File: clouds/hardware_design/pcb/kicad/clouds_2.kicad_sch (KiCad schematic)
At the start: 37 parts

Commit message: clouds wm8731 schematic update
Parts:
- IC8: value (none) -> WM8731; footprint (none) -> Package_DFN_QFN:QFN-28-1EP_5x5mm_P0.5mm_EP3.35x3.35mm
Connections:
- net +3V3: now also IC8.3 (DCVDD), IC8.5 (DBVDD); no longer IC8.1 (DBVDD), IC8.27 (DCVDD)
- net +3V3_A: now also IC8.12 (HPVDD), IC8.18 (AVDD); no longer IC8.14 (AVDD), IC8.8 (HPVDD)
- net GND: now also IC8.19 (AGND), IC8.25 (MODE), IC8.26 (CSB), IC8.4 (DGND); no longer IC8.11 (HPGND), IC8.21 (MODE), IC8.22 (CSB), IC8.28 (DGND)
- net I2C_SCL: now also IC8.28 (SCLK); no longer IC8.24 (SCLK)
- net I2C_SDA: now also IC8.27 (SDIN); no longer IC8.23 (SDIN)
- net I2S_LRCK: now also IC8.11 (ADCLRC), IC8.9 (DACLRC); no longer IC8.5 (DACLRC), IC8.7 (ADCLRC)
- net I2S_SCK: now also IC8.7 (BCLK); no longer IC8.3 (BCLK)
- net I2S_SIN: now also IC8.10 (ADCDAT); no longer IC8.6 (ADCDAT)
- net I2S_SOUT: now also IC8.8 (DACDAT); no longer IC8.4 (DACDAT)
- net LIN: now also IC8.24 (LLINEIN); no longer IC8.20 (LLINEIN)
- net LOUT: now also IC8.16 (LOUT); no longer IC8.12 (LOUT)
- net RIN: now also IC8.23 (RLINEIN); no longer IC8.19 (RLINEIN)
- net ROUT: now also IC8.17 (ROUT); no longer IC8.13 (ROUT)
- net at C48.2, Q4.2: now also IC8.1 (XTI/MCLK); no longer IC8.25 (XTI/MCLK)
- net at C47.2, Q4.1: now also IC8.2 (XTO); no longer IC8.26 (XTO)
- net at C34.1, C35.+: now also IC8.20 (VMID); no longer IC8.16 (VMID)
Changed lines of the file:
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@@
     (pin "6")
+  )
+  (symbol (lib_id "clouds-eagle-import:WM8731") (at 340.36 111.76 0) (unit 1)
+    (in_bom yes) (on_board yes)
+    (property "Reference" "IC8" (id 0) (at 327.66 85.09 0)
+      (effects (font (size 1.778 1.5113)) (justify left bottom))
+    )
+    (property "Value" "WM8731" (id 1) (at 340.36 111.76 0)
+      (effects (font (size 1.27 1.27)) hide)
+    )
+    (property "Footprint" "Package_DFN_QFN:QFN-28-1EP_5x5mm_P0.5mm_EP3.35x3.35mm" (id 2) (at 340.36 109.22 0)
+      (effects (font (size 1.27 1.27)) hide)
+    )
+    (property "Datasheet" "" (id 3) (at 340.36 111.76 0)
+      (effects (font (size 1.27 1.27)) hide)
+    )
+    (pin "1")
+    (pin "10")
+    (pin "11")
+    (pin "12")
+    (pin "13")
+    (pin "14")
+    (pin "15")
+    (pin "16")
+    (pin "17")
+    (pin "18")
+    (pin "19")
+    (pin "2")
+    (pin "20")
+    (pin "21")
+    (pin "22")
+    (pin "23")
+    (pin "24")
+    (pin "25")
+    (pin "26")
+    (pin "27")
+    (pin "28")
+    (pin "3")
+    (pin "4")
+    (pin "5")
+    (pin "6")
+    (pin "7")
+    (pin "8")
+    (pin "9")
   )
   (symbol (lib_id "clouds-eagle-import:EVQQ2") (at 71.12 187.96 0) (unit 1)
@@
     (pin "2")
   )
-  (symbol (lib_id "clouds-eagle-import:WM8731") (at 340.36 111.76 0) (unit 1)
-    (in_bom yes) (on_board yes)
-    (property "Reference" "IC8" (id 0) (at 327.66 85.09 0)
-      (effects (font (size 1.778 1.5113)) (justify left bottom))
-    )
-    (property "Value" "" (id 1) (at 340.36 111.76 0)
-      (effects (font (size 1.27 1.27)) hide)
-    )
-    (property "Footprint" "" (id 2) (at 340.36 111.76 0)
-      (effects (font (size 1.27 1.27)) hide)
-    )
-    (property "Datasheet" "" (id 3) (at 340.36 111.76 0)
-      (effects (font (size 1.27 1.27)) hide)
-    )
-    (pin "1")
-    (pin "10")
-    (pin "11")
-    (pin "12")
-    (pin "13")
-    (pin "14")
-    (pin "15")
-    (pin "16")
-    (pin "17")
-    (pin "18")
-    (pin "19")
-    (pin "2")
-    (pin "20")
-    (pin "21")
-    (pin "22")
-    (pin "23")
-    (pin "24")
-    (pin "25")
-    (pin "26")
-    (pin "27")
-    (pin "28")
-    (pin "3")
-    (pin "4")
-    (pin "5")
-    (pin "6")
-    (pin "7")
-    (pin "8")
-    (pin "9")
-  )
   (symbol (lib_id "clouds-eagle-import:C-USC0603") (at 195.58 200.66 0) (unit 1)

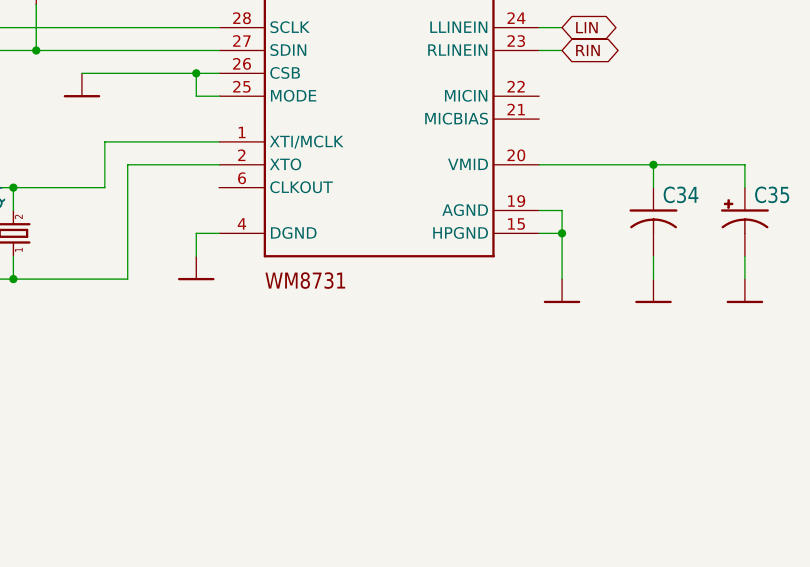
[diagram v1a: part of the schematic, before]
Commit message: clouds wm8731 QFN on PCB. also panasonic a -> b caps
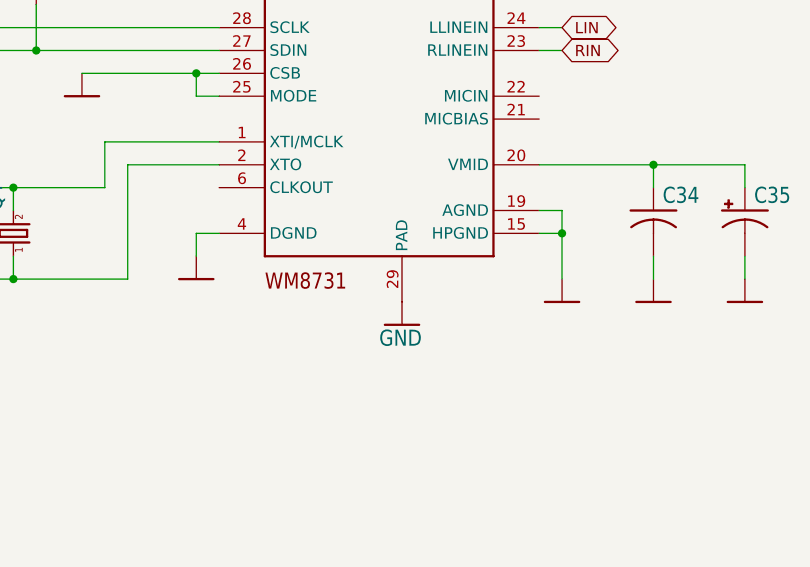
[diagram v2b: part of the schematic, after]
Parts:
- C28, C49: footprint (none) -> clouds:PANASONIC_B
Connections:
- net GND: now also IC8.29 (PAD)
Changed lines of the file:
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@@
+    (pin "1")
+  )
+  (symbol (lib_id "clouds-eagle-import:GND") (at 342.9 144.78 0) (unit 1)
+    (in_bom yes) (on_board yes)
+    (property "Reference" "#GND0101" (id 0) (at 342.9 144.78 0)
+      (effects (font (size 1.27 1.27)) hide)
+    )
+    (property "Value" "GND" (id 1) (at 340.36 147.32 0)
+      (effects (font (size 1.778 1.5113)) (justify left bottom))
+    )
+    (property "Footprint" "clouds:" (id 2) (at 342.9 144.78 0)
+      (effects (font (size 1.27 1.27)) hide)
+    )
+    (property "Datasheet" "" (id 3) (at 342.9 144.78 0)
+      (effects (font (size 1.27 1.27)) hide)
+    )
     (pin "1")
   )
@@
     (pin "3")
     (pin "4")
+    (pin "29")
     (pin "5")
     (pin "6")
@@
       (effects (font (size 1.778 1.5113)) (justify left bottom))
     )
-    (property "Footprint" "" (id 2) (at 215.9 200.66 0)
+    (property "Footprint" "clouds:PANASONIC_B" (id 2) (at 215.9 200.66 0)
       (effects (font (size 1.27 1.27)) hide)
     )
@@
       (effects (font (size 1.778 1.5113)) (justify left bottom))
     )
-    (property "Footprint" "" (id 2) (at 243.84 200.66 0)
-      (effects (font (size 1.27 1.27)) hide)
-    )
+    (property "Footprint" "clouds:PANASONIC_B" (id 2) (at 243.84 200.66 0)
+      (effects (font (size 1.27 1.27)) hide)
+    )

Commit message: clouds SMD reset + boot buttons
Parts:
- SW4, SW5: footprint (none) -> Supercell 1.3:k2-1808 pushbutton switch
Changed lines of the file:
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@@
       (effects (font (size 1.778 1.5113)) (justify left bottom))
     )
-    (property "Footprint" "" (id 2) (at 71.12 187.96 0)
+    (property "Footprint" "Supercell 1.3:k2-1808 pushbutton switch" (id 2) (at 71.12 187.96 0)
       (effects (font (size 1.27 1.27)) hide)
     )
@@
       (effects (font (size 1.778 1.5113)) (justify left bottom))
     )
-    (property "Footprint" "" (id 2) (at 73.66 160.02 0)
+    (property "Footprint" "Supercell 1.3:k2-1808 pushbutton switch" (id 2) (at 73.66 160.02 0)
       (effects (font (size 1.27 1.27)) hide)
     )

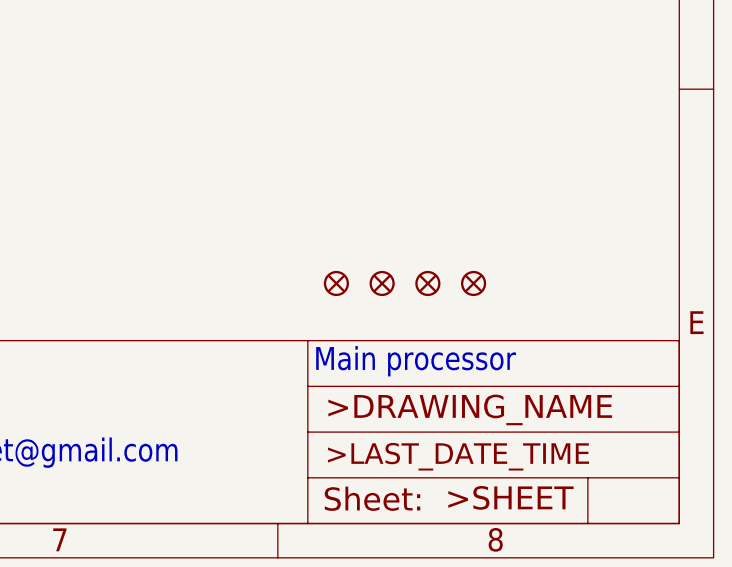
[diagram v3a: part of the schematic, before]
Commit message: clouds new kind of LED/switch pushbutton
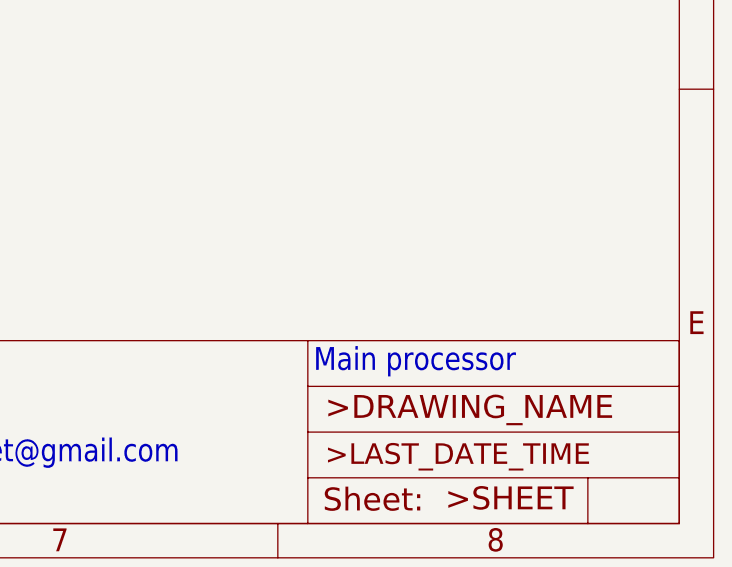
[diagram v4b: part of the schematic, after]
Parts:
- removed F1, F2, F3, F4: (no value), symbol clouds-eagle-import:FIDUCIAL1X2
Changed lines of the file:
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@@
     (pin "1")
-  )
-  (symbol (lib_id "clouds-eagle-import:FIDUCIAL1X2") (at 373.38 248.92 0) (unit 1)
-    (in_bom yes) (on_board yes)
-    (property "Reference" "F3" (id 0) (at 373.38 248.92 0)
-      (effects (font (size 1.27 1.27)) hide)
-    )
-    (property "Value" "" (id 1) (at 373.38 248.92 0)
-      (effects (font (size 1.27 1.27)) hide)
-    )
-    (property "Footprint" "" (id 2) (at 373.38 248.92 0)
-      (effects (font (size 1.27 1.27)) hide)
-    )
-    (property "Datasheet" "" (id 3) (at 373.38 248.92 0)
-      (effects (font (size 1.27 1.27)) hide)
-    )
   )
   (symbol (lib_id "clouds-eagle-import:CRYSTALHC49UP") (at 299.72 134.62 90) (unit 1)
@@
     (pin "1")
     (pin "2")
-  )
-  (symbol (lib_id "clouds-eagle-import:FIDUCIAL1X2") (at 378.46 248.92 0) (unit 1)
-    (in_bom yes) (on_board yes)
-    (property "Reference" "F2" (id 0) (at 378.46 248.92 0)
-      (effects (font (size 1.27 1.27)) hide)
-    )
-    (property "Value" "" (id 1) (at 378.46 248.92 0)
-      (effects (font (size 1.27 1.27)) hide)
-    )
-    (property "Footprint" "" (id 2) (at 378.46 248.92 0)
-      (effects (font (size 1.27 1.27)) hide)
-    )
-    (property "Datasheet" "" (id 3) (at 378.46 248.92 0)
-      (effects (font (size 1.27 1.27)) hide)
-    )
   )
   (symbol (lib_id "clouds-eagle-import:M06SIP") (at 68.58 101.6 0) (unit 1)
@@
     (pin "-")
   )
-  (symbol (lib_id "clouds-eagle-import:FIDUCIAL1X2") (at 363.22 248.92 0) (unit 1)
-    (in_bom yes) (on_board yes)
-    (property "Reference" "F4" (id 0) (at 363.22 248.92 0)
-      (effects (font (size 1.27 1.27)) hide)
-    )
-    (property "Value" "" (id 1) (at 363.22 248.92 0)
-      (effects (font (size 1.27 1.27)) hide)
-    )
-    (property "Footprint" "" (id 2) (at 363.22 248.92 0)
-      (effects (font (size 1.27 1.27)) hide)
-    )
-    (property "Datasheet" "" (id 3) (at 363.22 248.92 0)
-      (effects (font (size 1.27 1.27)) hide)
-    )
-  )
   (symbol (lib_id "clouds-eagle-import:C-USC0603") (at 256.54 162.56 270) (mirror x) (unit 1)
     (in_bom yes) (on_board yes)
@@
     (pin "1")
   )
-  (symbol (lib_id "clouds-eagle-import:FIDUCIAL1X2") (at 368.3 248.92 0) (unit 1)
-    (in_bom yes) (on_board yes)
-    (property "Reference" "F1" (id 0) (at 368.3 248.92 0)
-      (effects (font (size 1.27 1.27)) hide)
-    )
-    (property "Value" "" (id 1) (at 368.3 248.92 0)
-      (effects (font (size 1.27 1.27)) hide)
-    )
-    (property "Footprint" "" (id 2) (at 368.3 248.92 0)
-      (effects (font (size 1.27 1.27)) hide)
-    )
-    (property "Datasheet" "" (id 3) (at 368.3 248.92 0)
-      (effects (font (size 1.27 1.27)) hide)
-    )
-  )
   (symbol (lib_id "clouds-eagle-import:GND") (at 73.66 210.82 0) (mirror y) (unit 1)
